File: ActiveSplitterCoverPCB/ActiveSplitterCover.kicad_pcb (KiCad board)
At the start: 2 copper layers, 78 x 31 mm, 5 parts, among them J10 Conn_01x01_Pin, J6 Conn_01x28_Pin, J7 Conn_01x28_Pin, J8 Conn_01x12_Pin, J9 Conn_01x12_Pin

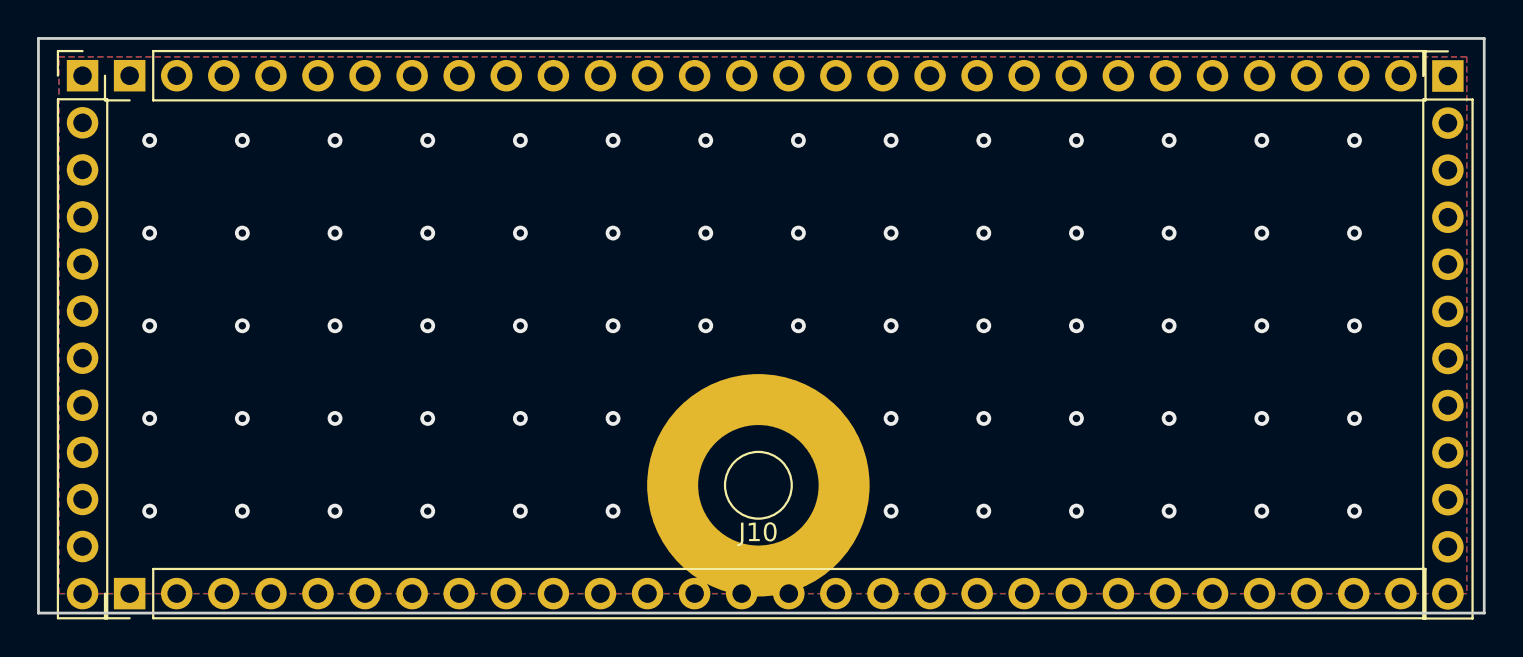
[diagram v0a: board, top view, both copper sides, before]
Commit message: update size of cover PCB
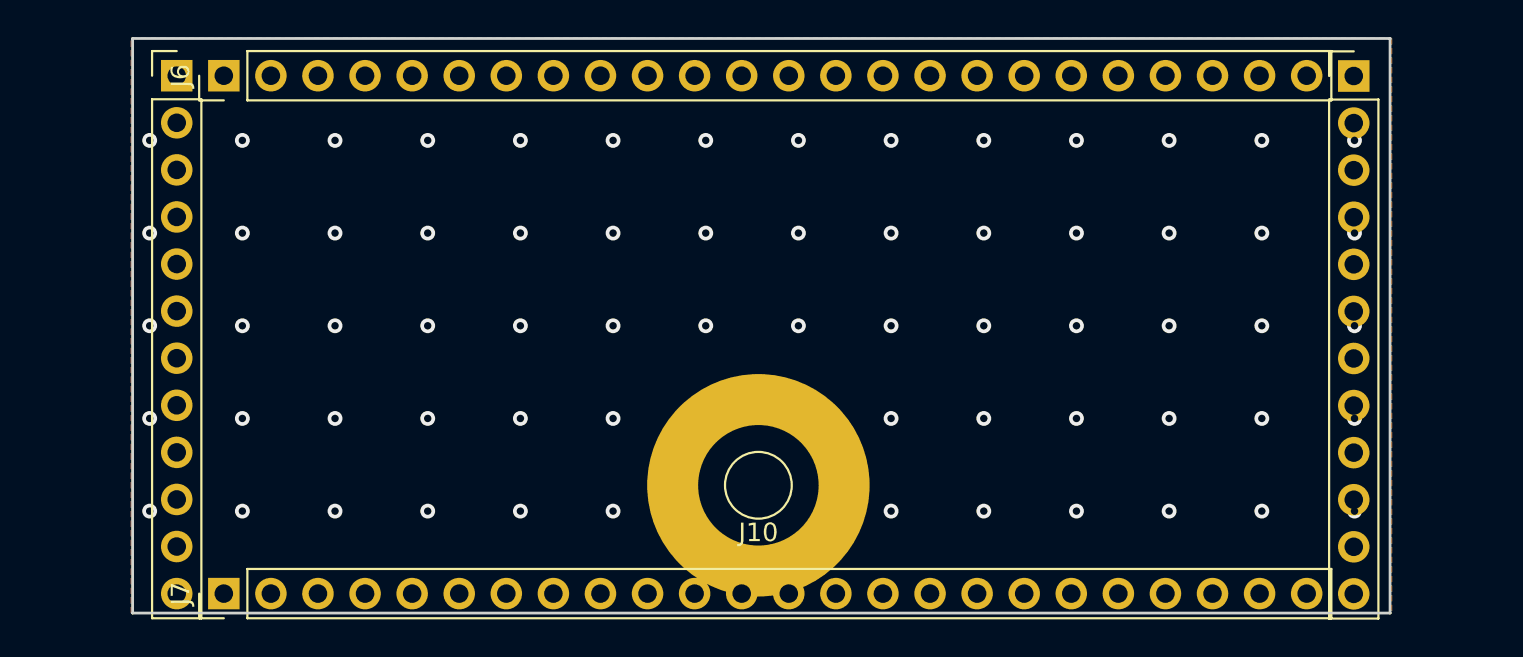
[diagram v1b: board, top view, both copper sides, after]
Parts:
- J6, J7: value Conn_01x28_Pin -> Conn_01x24_Pin; footprint Connector_PinHeader_2.54mm:PinHeader_1x28_P2.54mm_Vertical -> Connector_PinHeader_2.54mm:PinHeader_1x24_P2.54mm_Vertical
- moved J6 5.08 mm to (108.5, 83.3)
- moved J7 5.08 mm to (108.5, 111.2)
- moved J8 5.08 mm to (106.0, 83.3)
- moved J9 5.08 mm to (169.5, 83.3)
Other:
- board size 78 x 31 mm -> 67.8 x 31 mm
